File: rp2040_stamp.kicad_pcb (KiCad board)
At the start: 4 copper layers, 25 x 25 mm, 75 parts, among them J1 Conn_South, J2 Conn_North, J3 Conn_East, J4 Conn_West, Q1 BSS84, SW1 SW_RESET, U1 RP2040, U2 AP2112K-3.3, U3 W25Q64JV, U4 MCP73831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

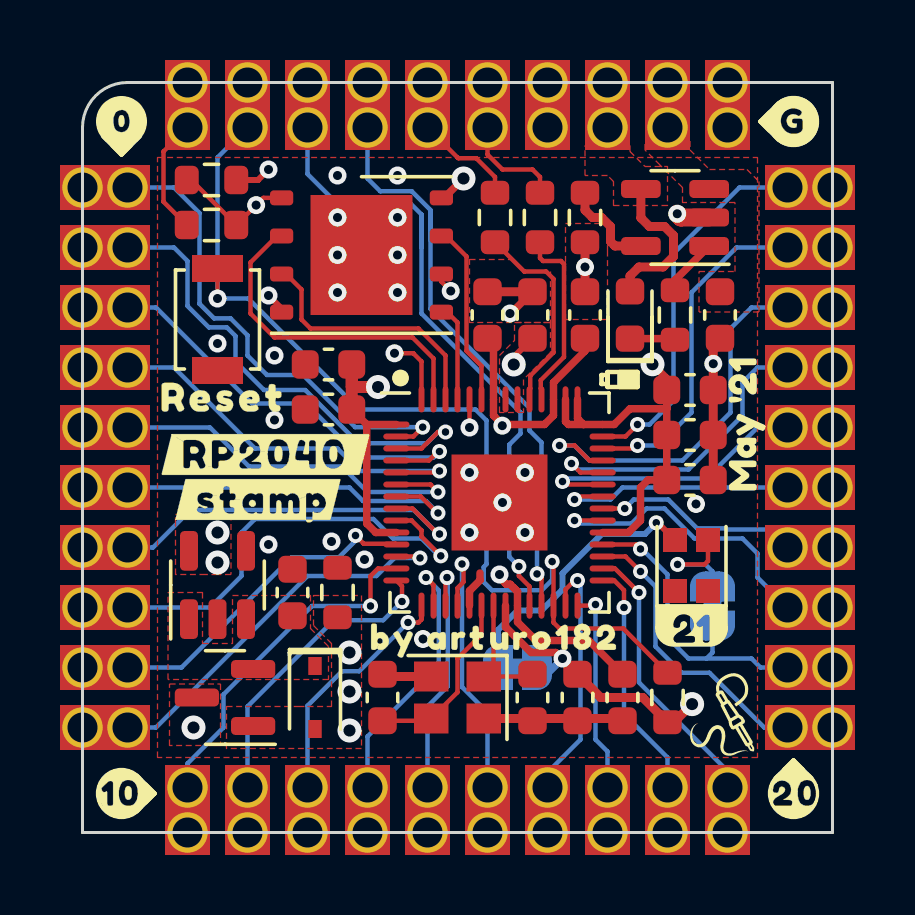
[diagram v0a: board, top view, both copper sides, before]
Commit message: Removed unnecessary parts to be cheaper to manufacture via JLC.
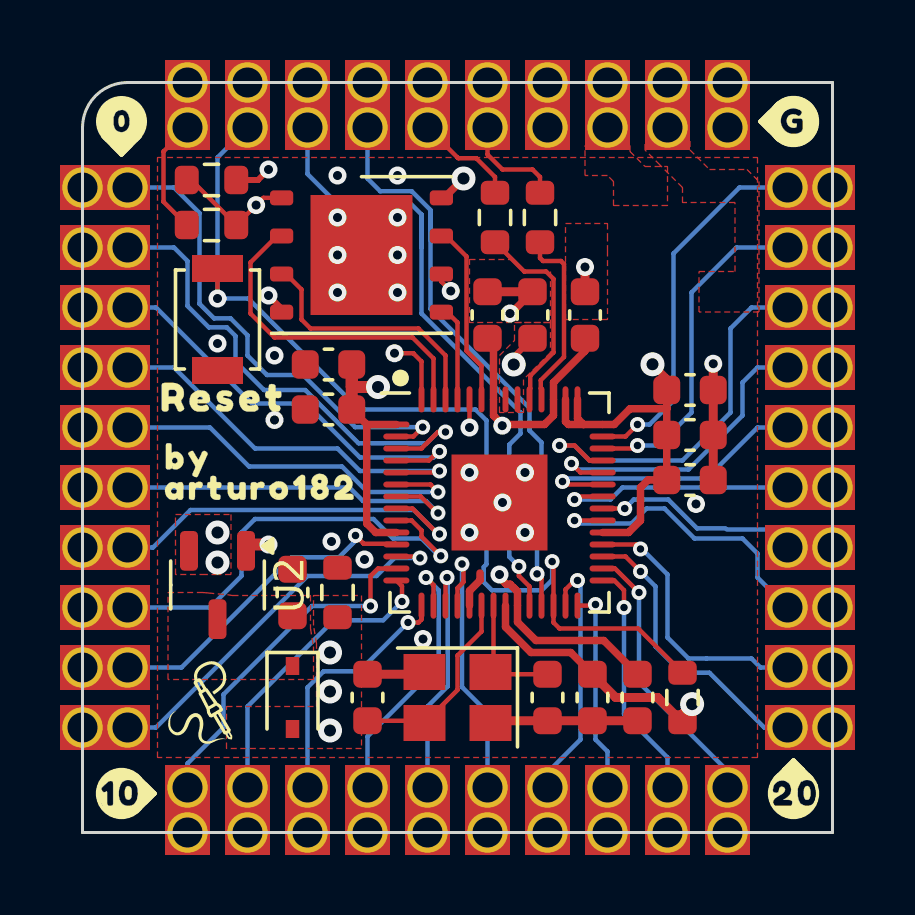
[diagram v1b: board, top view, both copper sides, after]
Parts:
- removed the ? at (144.8, 106.9)
- removed the ? at (160.0, 107.7)
- removed the ? at (145.1, 105.4)
- removed C16: 10uF, Capacitor_SMD:C_0603_1608Metric
- removed D2: LED_CHR, LED_SMD:LED_0603_1608Metric
- removed D3: WS2812B-2020, LED_SMD_Extra:WS2812B-2020
- removed JP1: Jumper_Neopixel_VDD, Jumper:SolderJumper-2_P1.3mm_Bridged_RoundedPad1.0x1.5mm
- removed JP2: Jumper_Neopixel, Jumper:SolderJumper-2_P1.3mm_Bridged_RoundedPad1.0x1.5mm
- removed Q1: BSS84, Package_TO_SOT_SMD:SOT-23
- removed R7: 2K, Resistor_SMD:R_0603_1608Metric
- removed R8: 1K, Resistor_SMD:R_0603_1608Metric
- removed U4: MCP73831, Package_TO_SOT_SMD:SOT-23-5
- removed the svg2mod at (161.2, 104.4)
- removed the svg2mod at (159.3, 111.2)
- removed the svg2mod at (158.5, 97.4)
- removed the svg2mod at (150.3, 112.0)
- U2: value AP2112K-3.3 -> XC6206P33; footprint Package_TO_SOT_SMD:SOT-23-5 -> Package_TO_SOT_SMD:SOT-23-3
- Y1: footprint Crystal:Crystal_SMD_2520-4Pin_2.5x2.0mm -> Crystal:Crystal_SMD_3225-4Pin_3.2x2.5mm
- moved G*** 17.4 mm to (143.2, 113.8)
- moved ? 10.1 mm to (144.0, 106.5)
- moved D1 0.75 mm to (146.0, 113.5)
- moved C11 0.50 mm to (157.5, 113.5)
- moved C14 0.50 mm to (148.5, 113.5)
- moved C15 0.50 mm to (154.5, 113.5)
- moved C3 0.50 mm to (156.0, 113.5)
- moved R2 0.50 mm to (159.0, 113.5)
- turned U2 to -90 degrees
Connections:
- U2 pad 1: /VIN -> GND
- U2 pad 2: GND -> +3V3
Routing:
- net VBAT: track 40.0 -> 0.00 mm, vias 1 -> 0
- net Net-(D3-Pad4): track 8.68 -> 0.00 mm, vias 1 -> 0
- net +5V: track 43.0 -> 38.4 mm
- net Net-(D3-Pad3): track 3.52 -> 0.00 mm, vias 1 -> 0
- net Net-(R7-Pad2): track 3.23 -> 0.00 mm
- net Net-(R8-Pad2): track 1.95 -> 0.00 mm
- net +3V3: track 35.7 -> 34.1 mm, vias 9 -> 8
- net Net-(D2-Pad1): track 1.52 -> 0.00 mm
- net GND: track 20.0 -> 18.5 mm, vias 26 -> 25
- net /GPIO21: track 10.3 -> 9.09 mm
- net Net-(U1-XIN): track 6.11 -> 6.63 mm
- net Net-(U1-VREG_VOUT): track 19.7 -> 20.2 mm
- net /~{RESET}: track 32.9 -> 33.4 mm

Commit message: Created production files.
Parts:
- removed the ? at (143.7, 103.5)
- removed SW1: SW_RESET, Button_Switch_SMD:SW_SPST_B3U-1000P
- moved ? 0.80 mm to (144.4, 105.8)
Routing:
- net /~{RESET}: track 33.4 -> 32.4 mm, vias 2 -> 1
- net GND: vias 25 -> 24
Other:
- board text added: "&カラスモッド"
